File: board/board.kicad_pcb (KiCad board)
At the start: 2 copper layers, 21 x 13 mm, 11 parts, among them J1 003_power, J2 003_power, J3 Conn_01x03_Male, U1 TLV743P

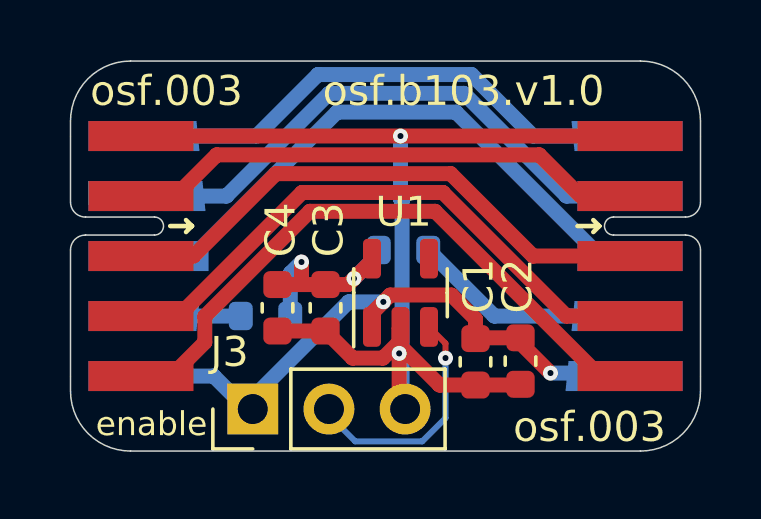
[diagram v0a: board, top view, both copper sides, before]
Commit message: modernized layout to use 000 generic power symbols. the layout and thereofore the hardware version number is unaffected
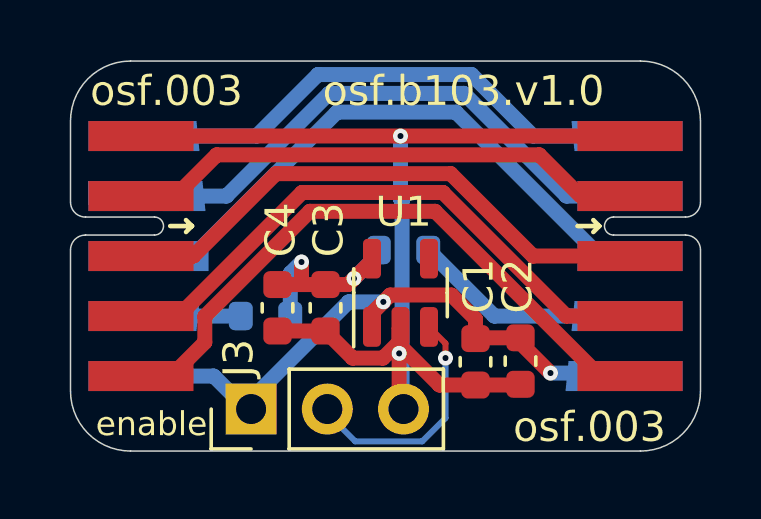
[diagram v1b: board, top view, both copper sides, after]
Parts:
- moved J3 0.05 mm to (146.0, 101.6)
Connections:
- net Net-(U1-Pad3) renamed /ldo/enable
